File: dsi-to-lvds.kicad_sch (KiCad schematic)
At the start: 20 parts, among them Q8 PJE138K, U2 NTS0104_DHVQFN, U3 SN65DSI84

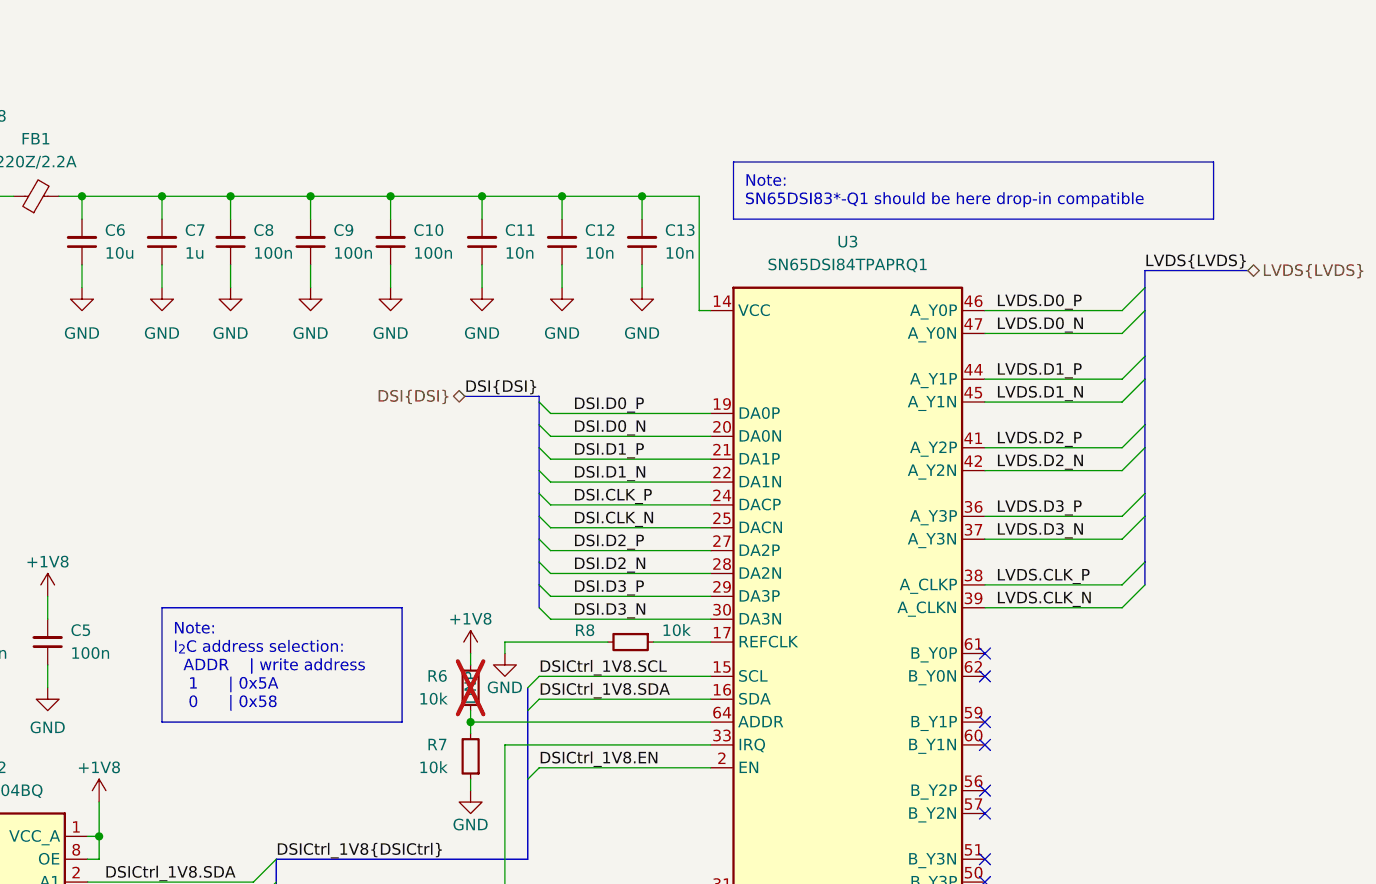
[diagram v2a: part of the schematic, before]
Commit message: [#58170] Change charge-pump caps; disable FDLY; update from lib
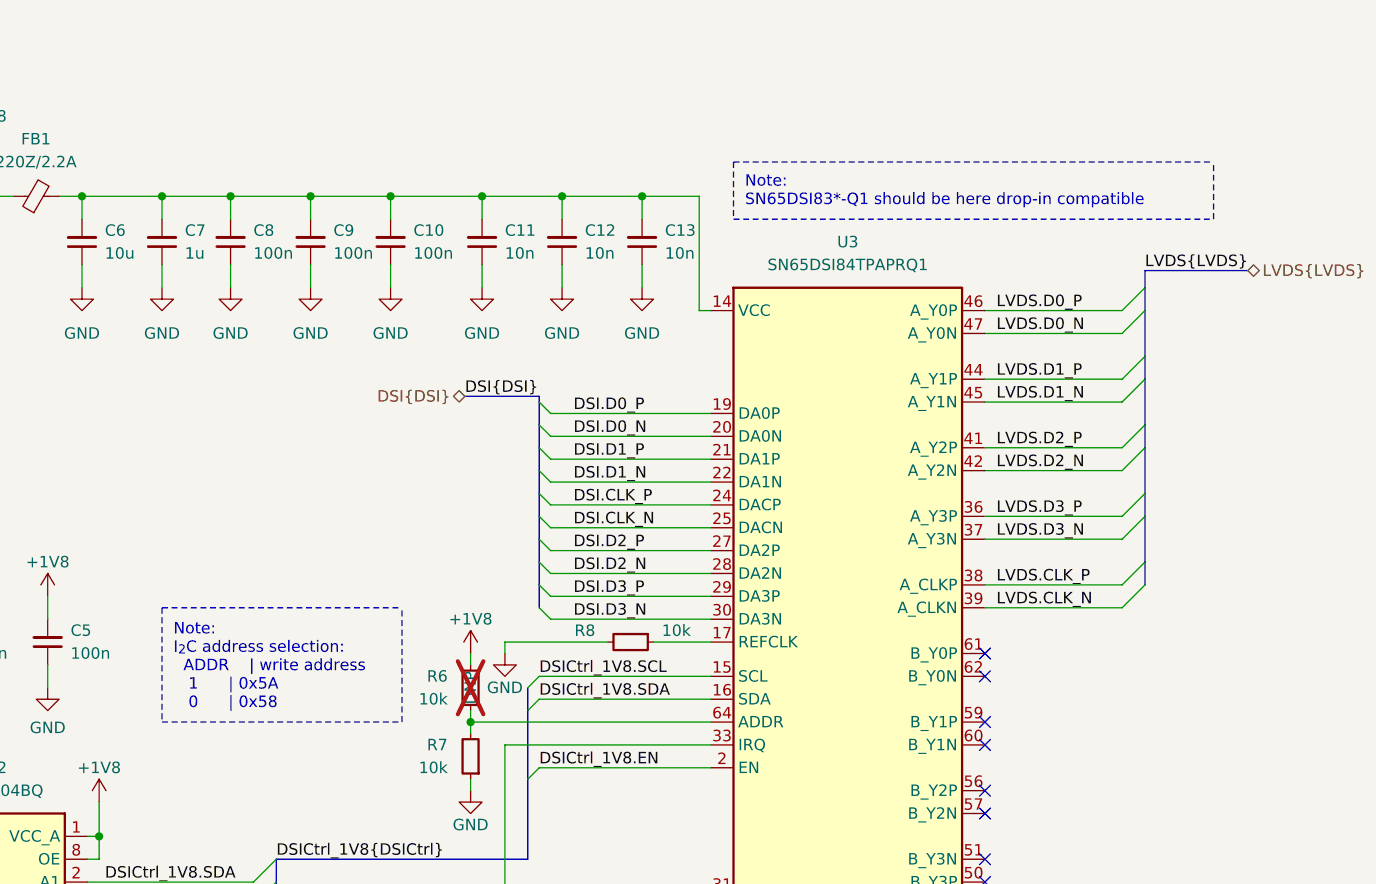
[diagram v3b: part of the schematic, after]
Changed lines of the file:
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@@
   )
   (polyline (pts (xy 195.58 54.61) (xy 248.92 54.61))
-    (stroke (width 0) (type default))
+    (stroke (width 0) (type dash))
   )
   (bus (pts (xy 173.99 95.25) (xy 173.99 97.79))
@@
   )
   (polyline (pts (xy 248.92 54.61) (xy 248.92 48.26))
-    (stroke (width 0) (type default))
+    (stroke (width 0) (type dash))
   )
   (wire (pts (xy 119.38 96.52) (xy 119.38 99.06))
@@
   )
   (polyline (pts (xy 132.08 110.49) (xy 158.75 110.49))
-    (stroke (width 0) (type default))
+    (stroke (width 0) (type dash))
   )
   (wire (pts (xy 165.735 160.02) (xy 165.735 159.385))
@@
   )
   (polyline (pts (xy 132.08 97.79) (xy 158.75 97.79))
-    (stroke (width 0) (type default))
+    (stroke (width 0) (type dash))
   )
   (wire (pts (xy 176.53 59.69) (xy 176.53 62.23))
@@
   )
   (polyline (pts (xy 158.75 110.49) (xy 158.75 97.79))
-    (stroke (width 0) (type default))
+    (stroke (width 0) (type dash))
   )
   (bus (pts (xy 172.72 106.68) (xy 172.72 109.22))
@@
   )
   (polyline (pts (xy 195.58 48.26) (xy 248.92 48.26))
-    (stroke (width 0) (type default))
+    (stroke (width 0) (type dash))
   )
   (wire (pts (xy 157.48 59.69) (xy 157.48 62.23))
@@
   )
   (polyline (pts (xy 195.58 48.26) (xy 195.58 54.61))
-    (stroke (width 0) (type default))
+    (stroke (width 0) (type dash))
   )
   (wire (pts (xy 139.7 52.07) (xy 132.08 52.07))
@@
   )
   (polyline (pts (xy 132.08 97.79) (xy 132.08 110.49))
-    (stroke (width 0) (type default))
+    (stroke (width 0) (type dash))
   )
   (wire (pts (xy 107.95 96.52) (xy 107.95 99.06))
